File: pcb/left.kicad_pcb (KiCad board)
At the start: 2 copper layers, 135 x 95.7 mm, 56 parts, among them SW1 SW_PUSH, SW10 SW_PUSH, SW11 SW_PUSH, SW12 SW_PUSH, SW13 SW_PUSH, SW14 SW_PUSH, SW15 SW_PUSH, SW16 SW_PUSH, SW17 SW_PUSH, SW18 SW_PUSH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

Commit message: add full version
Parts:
- removed BATTSW2: SW_SPDT, Button_Switch_SMD:SW_SPDT_PCM12
- removed LED1: YS-SK6812MINI-E, pica:SK6812-MINI-E
- removed OLED1: OLED, kbd:OLED_v2
- removed RESET1: SW_Push, kbd:ResetSW_1side
- removed Ue: ProMicro_r, pica:ProMicro
- added RE1: RotaryEncoder_Switch, pica:RotaryEncoder_EC11, F.Cu at (192.6, 96.8)
- added U1: xiao-ble, kleeb-mcu:xiao-ble-tht, F.Cu at (193.0, 70.5)
- added wired: SolderJumper_2_Open, Jumper:SolderJumper-2_P1.3mm_Open_TrianglePad1.0x1.5mm, F.Cu at (183.8, 85.2)
- added wireless: SolderJumper_2_Open, Jumper:SolderJumper-2_P1.3mm_Open_TrianglePad1.0x1.5mm, B.Cu at (183.8, 85.2)
- USB1: footprint typec:HRO-TYPE-C-31-M-12-HandSoldering -> pica:HRO-TYPE-C-31-M-12-data
- moved BATTSW1 29.5 mm to (200.9, 85.8), turned to 90 degrees
- moved BATTCONN1 11.0 mm to (196.4, 85.0)
- moved USB1 0.57 mm to (203.5, 114.0)
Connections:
- USB1 pad 1: ENCB -> GND
- USB1 pad 11: row7 -> VCC
- USB1 pad 2: ENCA -> VCC
- USB1 pad 5: col2 -> ENCB
- USB1 pad 6: col3 -> DATA
- USB1 pad 7: col4 -> ENCB
- USB1 pad 8: row4 -> DATA
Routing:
- net col0: track 335.6 -> 154.3 mm
- net col1: track 249.2 -> 178.0 mm
- net col3: track 158.9 -> 103.4 mm
- net row7: track 55.5 -> 0.00 mm
- net col2: track 174.7 -> 120.1 mm
- net row6: track 53.6 -> 0.00 mm
- net row5: track 51.7 -> 0.00 mm
- net LED: track 50.0 -> 0.00 mm
- net row4: track 49.8 -> 0.00 mm
- net col4: track 116.2 -> 69.1 mm
- net BATT: track 46.4 -> 3.07 mm, vias 1 -> 0
- net DATA: track 0.00 -> 37.0 mm, vias 0 -> 2
- net RESET: track 36.0 -> 0.00 mm
- net ENCA: track 57.2 -> 22.0 mm
- net SDA: track 27.6 -> 0.00 mm
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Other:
- outline, holes or cut-outs redrawn

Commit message: v2
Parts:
- removed wired, wireless: SolderJumper_2_Open, Jumper:SolderJumper-2_P1.3mm_Open_TrianglePad1.0x1.5mm
- added BATTCONN2: Conn_01x02_Female, pica:JST_PH_S2B-PH-K_1x02_P2.00mm, F.Cu at (118.8, 105.5)
- added JP1: SolderJumper_2_Open, Jumper:SolderJumper-2_P1.3mm_Open_TrianglePad1.0x1.5mm, B.Cu at (168.6, 85.2)
- added JP2: SolderJumper_2_Open, Jumper:SolderJumper-2_P1.3mm_Open_TrianglePad1.0x1.5mm, F.Cu at (168.6, 85.2)
- added RE2: RotaryEncoder_Switch, pica:RotaryEncoder_EC11, F.Cu at (106.0, 117.2)
- BATTCONN1: footprint Connector_JST:JST_PH_S2B-PH-K_1x02_P2.00mm_Horizontal -> pica:JST_PH_S2B-PH-K_1x02_P2.00mm
- G***: moved to B.Cu
- H1, H2, H3, H4, H5: footprint kbd:M2_HOLE_v2 -> pica:spacer_m2_3.4
- H6, H7: footprint kbd:M2_Hole_TH -> kbd:thread_m2
- SW1, SW10, SW11, SW12, SW13, SW14, SW15, SW16, SW17, SW18, SW19, SW2, SW3, SW4, SW5, SW6, SW7, SW8, SW9: footprint pica:CherryMX_Hotswap -> pica:CherryMX_Hotswap_ChocV2
- SW20: footprint pica:CherryMX_Hotswap_1.5 -> pica:CherryMX_Hotswap_ChocV2_1.5
- U1: footprint kleeb-mcu:xiao-ble-tht -> pica:xiao-ble-tht
- moved H7 35.0 mm to (177.6, 78.5)
- moved H6 33.0 mm to (168.8, 78.5)
- moved SW1 21.9 mm to (75.6, 71.4), turned to 5 degrees
- moved D1 21.3 mm to (76.2, 79.4), turned to -175 degrees
- moved H1 21.0 mm to (87.1, 69.0)
- moved SW16 20.9 mm to (57.8, 86.6), turned to 5 degrees
- moved SW6 20.3 mm to (77.2, 90.3), turned to 5 degrees
- moved D16 20.1 mm to (58.6, 94.6), turned to -175 degrees
- moved H3 20.1 mm to (67.5, 95.2), turned to 5 degrees
- moved D17 19.9 mm to (58.8, 97.1), turned to -175 degrees
- moved D6 19.7 mm to (77.9, 98.3), turned to -175 degrees
- moved D11 19.5 mm to (78.1, 100.8), turned to -175 degrees
- moved D18 19.4 mm to (125.8, 108.5)
- moved BATTSW1 19.4 mm to (182.3, 80.5)
- moved D12 19.4 mm to (97.8, 105.5)
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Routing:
- net BATT: track 3.07 -> 139.9 mm
- net ENCA: track 22.0 -> 136.0 mm
- net ENCB: track 45.6 -> 111.9 mm, vias 0 -> 1
- net col0: track 154.3 -> 208.8 mm, vias 4 -> 0
- net col4: track 69.1 -> 115.0 mm, vias 4 -> 0
- net col3: track 103.4 -> 148.0 mm, vias 4 -> 0
- net col2: track 120.1 -> 158.9 mm, vias 4 -> 0
- net col1: track 178.0 -> 210.6 mm, vias 4 -> 0
- net Net-(D20-Pad2): track 20.3 -> 28.7 mm
- net Net-(D17-Pad2): track 8.61 -> 16.9 mm
- net Net-(D19-Pad2): track 6.89 -> 15.0 mm
- net Net-(D18-Pad2): track 8.37 -> 16.4 mm
- net Net-(D11-Pad2): track 8.47 -> 16.5 mm
- net row0: track 114.5 -> 122.4 mm
- net row1: track 128.0 -> 135.4 mm
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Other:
- board size 135 x 95.7 mm -> 137.8 x 95.7 mm
- board text added: "B+"
- board text added: "OFF"
- board text added: "Pica40 v2"
- board text added: "wired"
- board text added: "wireless"
- board text removed: "JLCJLCJLCJLC"
- board text removed: "PicaPica"

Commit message: remove second encoder
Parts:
- removed RE2: RotaryEncoder_Switch, pica:RotaryEncoder_EC11
- added G***: LOGO, pica:logo_mirror, F.Cu at (103.5, 114.6)
- moved BATTCONN2 2.28 mm to (121.0, 104.8)
- moved G*** 1.34 mm to (103.5, 114.6)
- moved BATTCONN1 0.05 mm to (178.2, 83.0)
- moved BATTSW1 0.05 mm to (182.2, 80.5)
- moved D1 0.05 mm to (76.1, 79.4)
- moved D10 0.05 mm to (154.8, 89.0)
- moved D14 0.05 mm to (135.8, 106.0)
- moved D15 0.05 mm to (154.8, 108.0)
- moved D19 0.05 mm to (144.8, 109.5)
- moved D20 0.05 mm to (168.9, 110.3)
- moved D4 0.05 mm to (135.8, 68.0)
- moved D5 0.05 mm to (154.8, 70.0)
- moved D9 0.05 mm to (135.8, 87.0)
- moved H2 0.05 mm to (159.8, 117.5)
- moved H5 0.05 mm to (146.2, 71.5)
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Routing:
- net ENCA: track 136.0 -> 28.0 mm
- net ENCB: track 111.9 -> 36.6 mm, vias 1 -> 0
- net BATT: track 139.9 -> 134.8 mm
- net col2: track 158.9 -> 161.1 mm
- net row2: track 147.0 -> 146.2 mm
- net col0: track 208.8 -> 208.1 mm
- net GND: vias 2 -> 3
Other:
- outline, holes or cut-outs redrawn

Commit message: udpate pcb, remove unused files
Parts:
- added G***: LOGO, pica:seeed-logo, F.Cu at (180.2, 83.2)
- added J1: MJ-4PP-9, pica:MJ-4PP-9_1side, F.Cu at (191.7, 90.0)
- added JP3: SolderJumper_2_Open, Jumper:SolderJumper-2_P1.3mm_Open_TrianglePad1.0x1.5mm, F.Cu at (176.0, 87.8)
- BATTSW1, JP2: moved to B.Cu
- JP1: moved to F.Cu
- moved BATTCONN1 11.5 mm to (188.4, 88.2)
- moved JP2 7.91 mm to (176.0, 87.8)
- moved BATTCONN2 7.66 mm to (128.3, 106.9)
- moved G*** 7.64 mm to (110.8, 116.9) (x2)
- moved D1 7.59 mm to (83.4, 81.6)
- moved D10 7.59 mm to (162.0, 91.2)
- moved D11 7.59 mm to (85.3, 103.0)
- moved D12 7.59 mm to (105.0, 107.8)
- moved D13 7.59 mm to (124.0, 103.8)
- moved D14 7.59 mm to (143.0, 108.3)
- moved D15 7.59 mm to (162.0, 110.2)
- moved D16 7.59 mm to (65.8, 96.8)
- moved D17 7.59 mm to (66.0, 99.3)
- moved D18 7.59 mm to (133.0, 110.8)
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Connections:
- JP1 pad 2: Net-(JP1-Pad2) -> ENCA
- JP2 pad 1: DATA -> ENCB
- JP2 pad 2: Net-(JP1-Pad2) -> Net-(U1-Pad7)
- U1 pad 7: Net-(JP1-Pad2) -> Net-(U1-Pad7)
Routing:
- net ENCB: track 36.6 -> 56.9 mm, vias 0 -> 1
- net VCC: track 60.3 -> 76.4 mm
- net Net-(JP1-Pad2): track 12.9 -> 0.00 mm, vias 1 -> 0
- net Net-(U1-Pad7): track 0.00 -> 12.6 mm, vias 0 -> 1
- net row3: track 180.1 -> 189.0 mm
- net BATT: track 134.8 -> 138.8 mm
- net RAW: track 19.3 -> 22.7 mm, vias 0 -> 1
- net DATA: track 33.6 -> 36.3 mm
- net ENCA: track 28.0 -> 29.8 mm
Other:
- outline, holes or cut-outs redrawn
- board text added: "JLCJLCJLCJLC"
- board text added: "no enc"

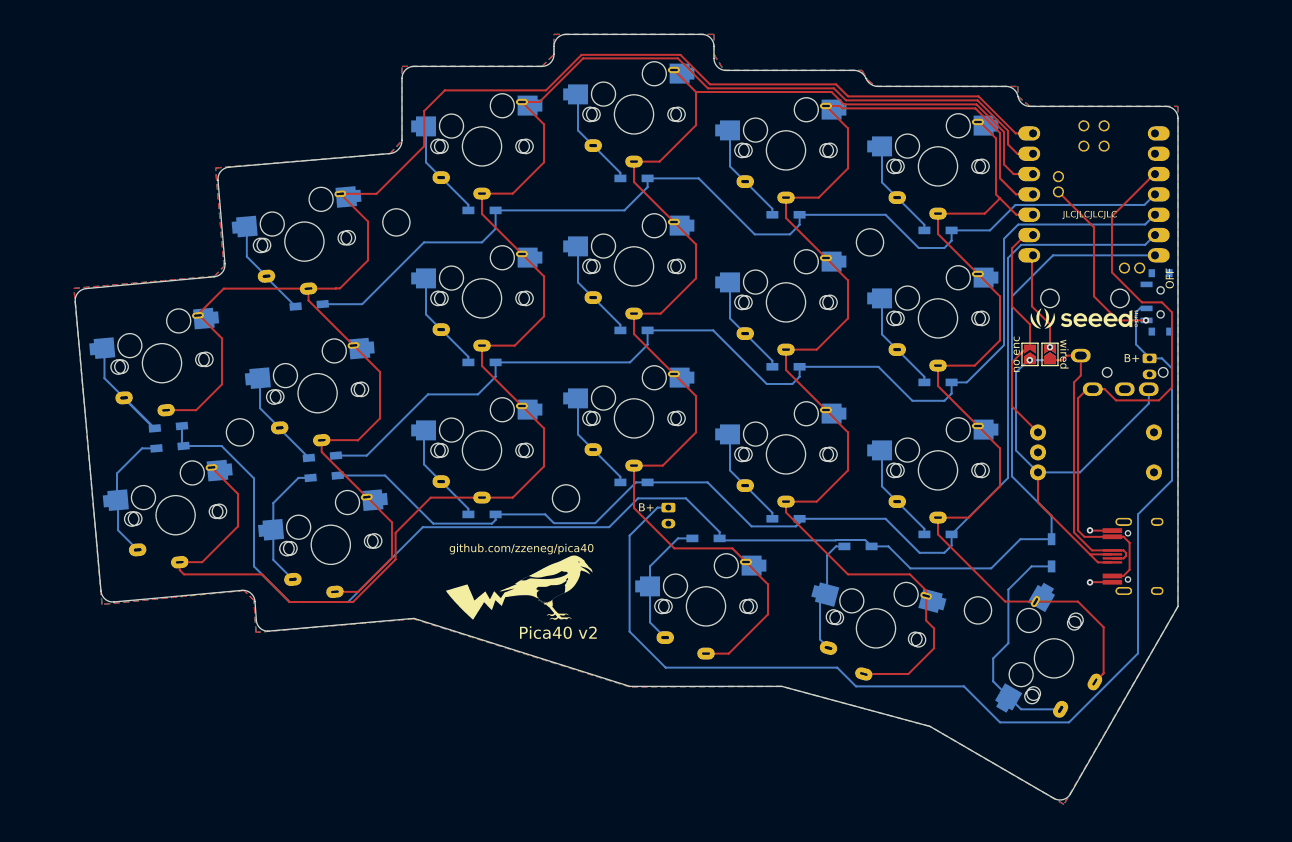
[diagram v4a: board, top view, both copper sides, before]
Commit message: improve footprints and routing
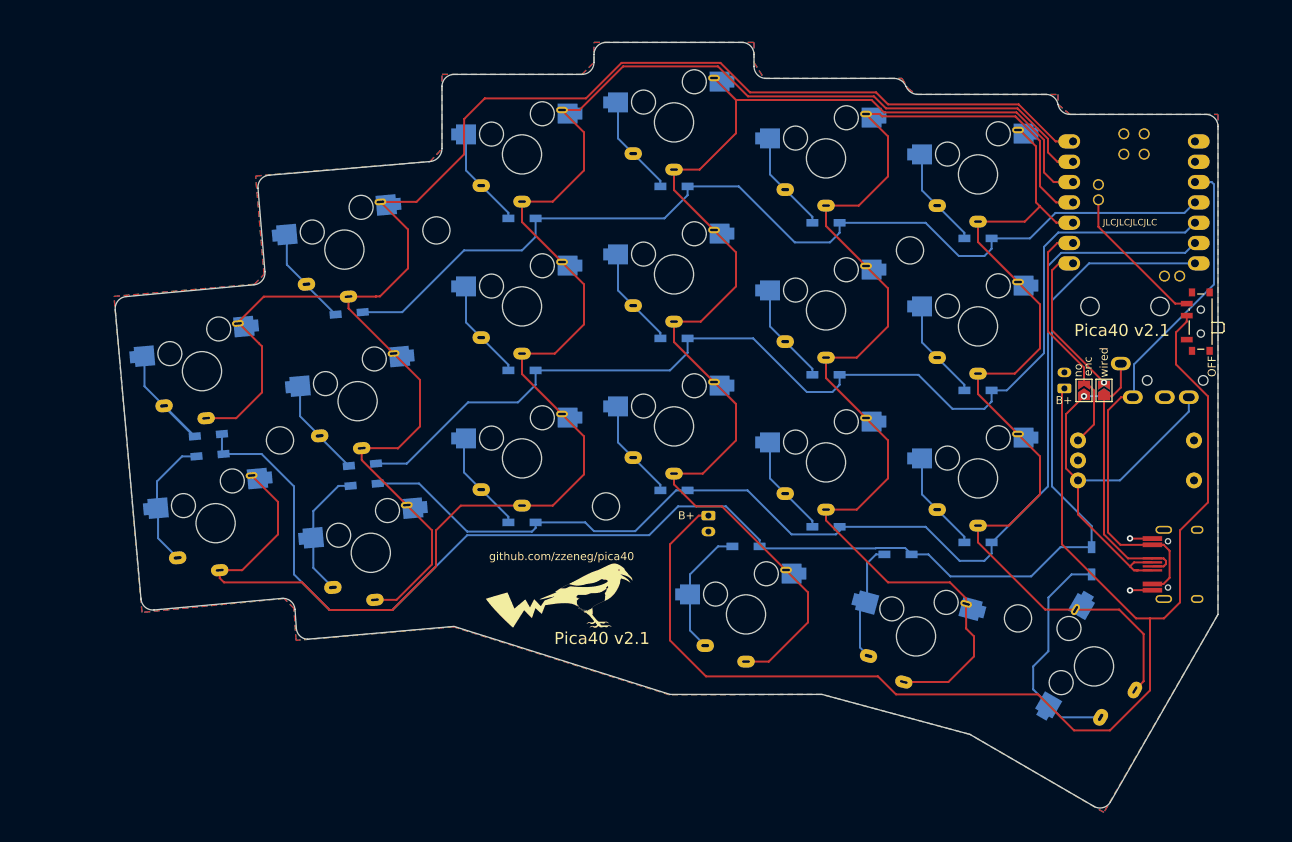
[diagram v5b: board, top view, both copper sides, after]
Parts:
- removed the G*** at (180.2, 83.2)
- BATTSW1: moved to F.Cu
- moved BATTCONN1 11.3 mm to (177.8, 92.0), turned to 90 degrees
- moved JP1 8.11 mm to (180.2, 92.2)
- moved JP2 8.11 mm to (182.8, 92.2)
- moved JP3 8.11 mm to (182.8, 92.2)
- moved BATTSW1 5.57 mm to (194.5, 83.7), turned to 90 degrees
- moved BATTCONN2 5.10 mm to (133.3, 107.9)
- moved D1 5.10 mm to (88.4, 82.6)
- moved D10 5.10 mm to (167.0, 92.2)
- moved D11 5.10 mm to (90.3, 104.0)
- moved D12 5.10 mm to (110.0, 108.8)
- moved D13 5.10 mm to (129.0, 104.8)
- moved D14 5.10 mm to (148.0, 109.3)
- moved D15 5.10 mm to (167.0, 111.2)
- moved D16 5.10 mm to (70.8, 97.8)
- moved D17 5.10 mm to (71.0, 100.3)
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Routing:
- net BATT: track 138.8 -> 172.6 mm
- net VCC: track 76.4 -> 66.8 mm
- net Net-(JP2-Pad2): track 12.6 -> 19.7 mm
- net RAW: track 22.7 -> 18.4 mm, vias 1 -> 0
- net ENCB: track 56.9 -> 53.5 mm
- net col2: track 160.9 -> 158.6 mm
- net DATA: track 36.3 -> 34.2 mm
- net ENCA: track 29.8 -> 30.6 mm
- net col1: track 211.3 -> 212.0 mm
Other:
- board text added: "Pica40 v2.1"
- board text added: "enc"
- board text added: "no"
- board text removed: "Pica40 v2"
- board text removed: "no enc"
